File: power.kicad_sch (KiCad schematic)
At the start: 65 parts, among them J5 S7B-XH-A

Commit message: schematic done
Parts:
- removed R34: 0.1m, symbol Device:R
- added BT1: Battery, symbol Device:Battery
- added R34: WSBS8518L1000JK, WSBS8518_VIS, symbol 2026-08-04_01-41-37:WSBS8518L1000JK
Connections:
- net BP-C1M is gone; now on net GND: C54.1, D4.1, J5.7, R20.2, R32.2
- net GND: now also BT1.2 (-), R34.1
- net Pack-: now also R34.2
- net VBAT_24V renamed Pack_24V
- net Pack_24V: now also BT1.1 (+)
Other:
- note added: "Battery plus directly connects to Pack plus"
- note removed: "Pin order needed to be checked"
- note removed: "UPDATE R SHUNT INFO"

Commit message: start to PCB drawing, but error due to missing footprint
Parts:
- R34: footprint WSBS8518_VIS -> MyFootLib:WSBS8518L1000JK
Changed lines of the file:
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@@
 			)
 		)
-		(property "Footprint" "WSBS8518_VIS"
+		(property "Footprint" "MyFootLib:WSBS8518L1000JK"
 			(at 203.2 113.03 0)
 			(hide yes)

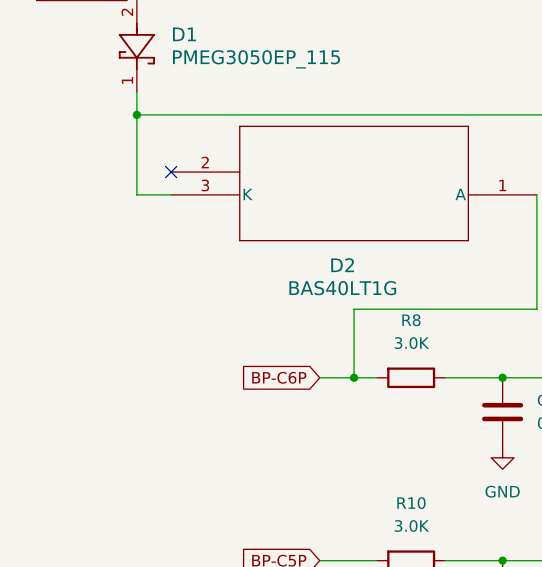
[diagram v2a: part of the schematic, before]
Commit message: feat: CAN/BUCK
1. CAN transceiver added
2. Buck added 24V -> 5V
3. LDO 5V -> 3.3V
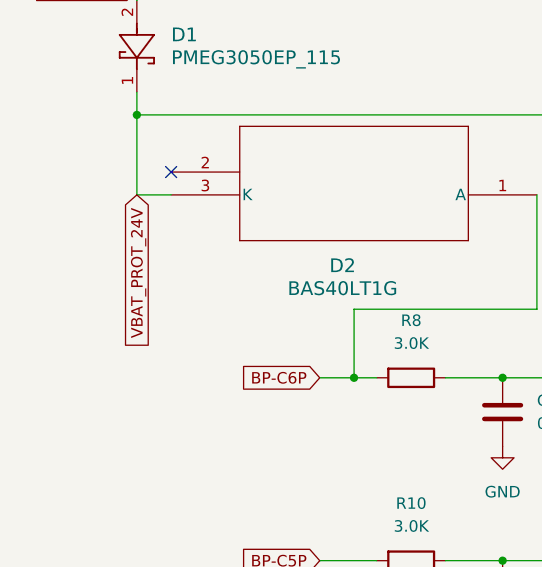
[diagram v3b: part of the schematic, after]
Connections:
- net VBAT_PROT_24V: now reaches C26.1, D1.1, D2.3 (K), R7.1
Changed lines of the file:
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@@
+		)
+	)
+	(global_label "VBAT_PROT_24V"
+		(shape input)
+		(at 26.67 43.18 270)
+		(fields_autoplaced yes)
+		(effects
+			(font
+				(size 1.27 1.27)
+			)
+			(justify right)
+		)
+		(property "Intersheetrefs" "${INTERSHEET_REFS}"
+			(at 26.67 60.8609 90)
+			(hide yes)
+			(show_name no)
+			(do_not_autoplace no)
+			(effects
+				(font
+					(size 1.27 1.27)
+				)
+				(justify right)
+			)
 		)
 	)

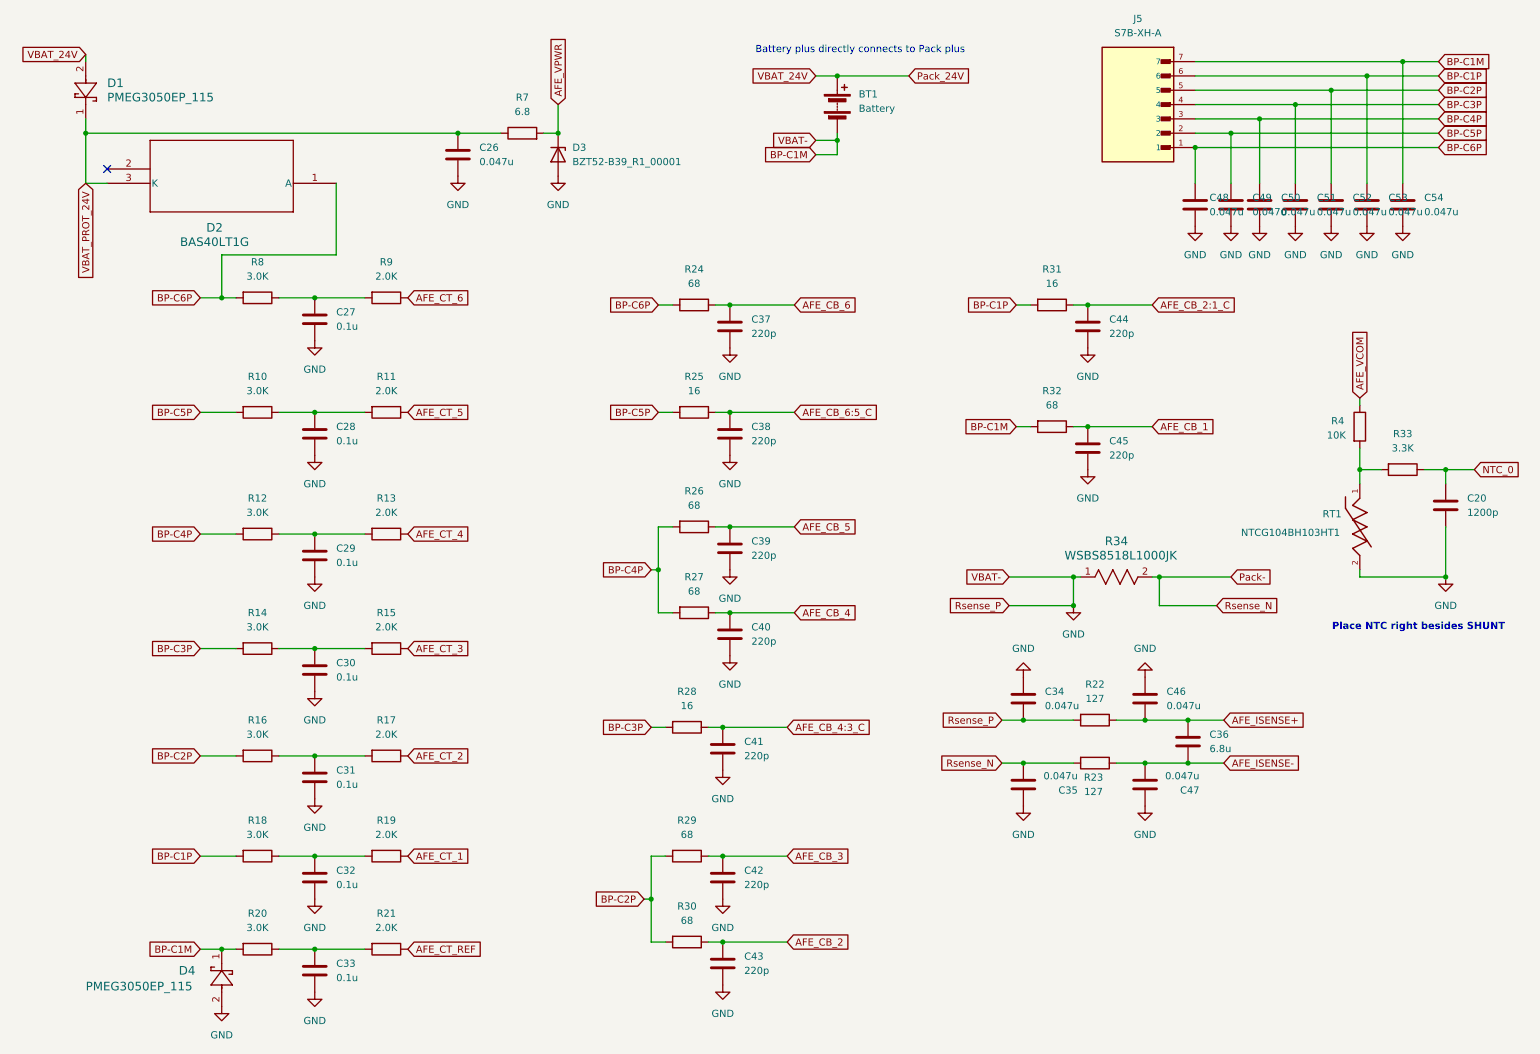
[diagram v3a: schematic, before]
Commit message: fullup the annotation for update PCB from Schematics
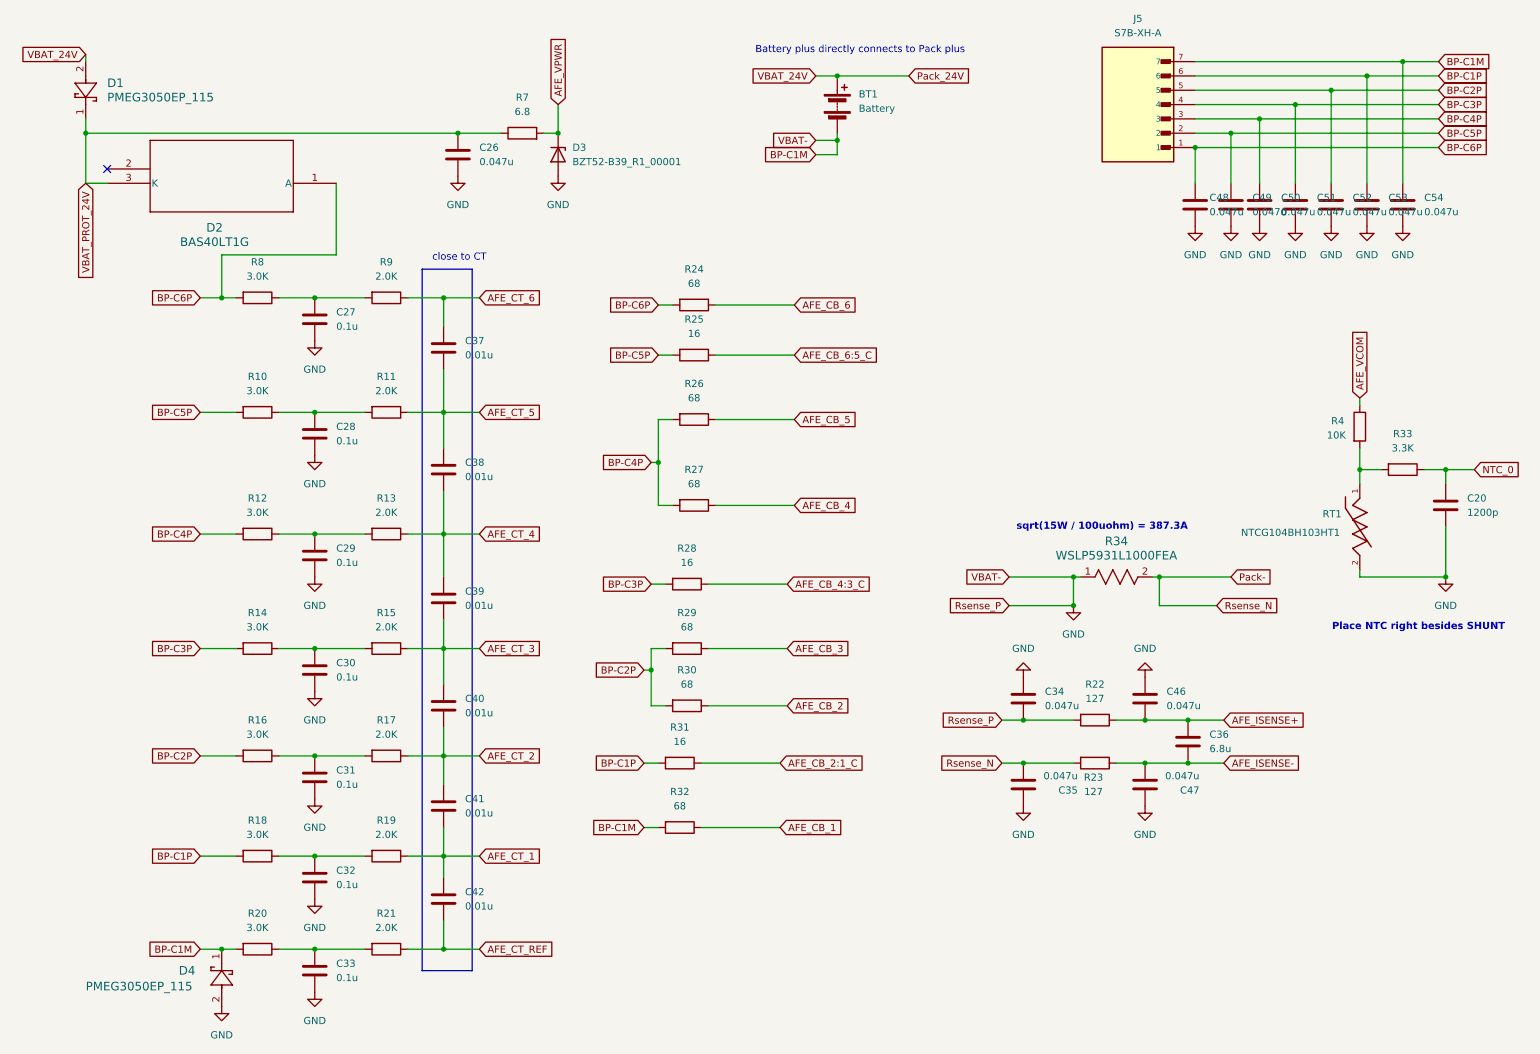
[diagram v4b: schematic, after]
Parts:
- removed C43, C44, C45: 220p, symbol Device:C
- removed R34: WSBS8518L1000JK, MyFootLib:WSBS8518L1000JK, symbol 2026-08-04_01-41-37:WSBS8518L1000JK
- added R34: WSLP5931L1000FEA, WSLP5931L1000FEA, symbol MySym:WSLP5931L1000FEA
- BT1: now left out of the parts list
- C20, C26, C27, C28, C29, C30, C31, C32, C33, C34, C35, C46, C47, C48, C49, C50, C51, C52, C53, C54: footprint (none) -> Capacitor_SMD:C_0402_1005Metric
- C36: footprint (none) -> Capacitor_SMD:C_0603_1608Metric
- C37, C38, C39, C40, C41, C42: value 220p -> 0.01u; footprint (none) -> Capacitor_SMD:C_0402_1005Metric
- D1, D4: footprint SDO_CFP5_SOD128_NEX -> MyFootLib:PMEG3050EP_115
- D2: footprint SOT-23-3_1P4X3P040_ONS -> MyFootLib:BAS40LT1
- J5: footprint S7B-XH-A:JST_S7B-XH-A -> MyFootLib:JST_S7B-XH-A
- R10, R11, R12, R13, R14, R15, R16, R17, R18, R19, R20, R21, R8, R9: footprint (none) -> Resistor_SMD:R_4020_10251Metric
- R22, R23, R33, R4: footprint (none) -> Resistor_SMD:R_0402_1005Metric
- R24, R25, R26, R27, R28, R29, R30, R31, R32: footprint (none) -> Resistor_SMD:R_1206_3216Metric
- R7: footprint (none) -> Resistor_SMD:R_0603_1608Metric
- RT1: footprint NTCG104BH103HT1:THERM_NTCG104BH103HT1 -> MyFootLib:THERM_NTCG104BH103HT1
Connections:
- net AFE_CB_3: no longer C42.1
- net AFE_CB_4: no longer C40.1
- net AFE_CB_4:3_C: no longer C41.1
- net AFE_CB_5: no longer C39.1
- net AFE_CB_6: no longer C37.1
- net AFE_CB_6:5_C: no longer C38.1
- net AFE_CT_1: now also C41.2, C42.1
- net AFE_CT_2: now also C40.2, C41.1
- net AFE_CT_3: now also C39.2, C40.1
- net AFE_CT_4: now also C38.2, C39.1
- net AFE_CT_5: now also C37.2, C38.1
- net AFE_CT_6: now also C37.1
- net AFE_CT_REF: now also C42.2
- net GND: now also R34.1; no longer C37.2, C38.2, C39.2, C40.2, C41.2, C42.2
- net Pack-: now also R34.2
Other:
- note added: "close to CT"
- note added: "sqrt(15W / 100uohm) = 387.3A"
- moved on the sheet: R25, R26, R27, R28, R29, R30, R31, R32

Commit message: update annotation
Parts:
- R34: footprint WSLP5931L1000FEA -> MyFootLib:WSLP5931L1000FEA
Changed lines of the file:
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@@
 			)
 		)
-		(property "Footprint" "WSLP5931L1000FEA"
+		(property "Footprint" "MyFootLib:WSLP5931L1000FEA"
 			(at 203.2 113.03 0)
 			(hide yes)

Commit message: correct R to 0402
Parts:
- R10, R11, R12, R13, R14, R15, R16, R17, R18, R19, R20, R21, R8, R9: footprint Resistor_SMD:R_4020_10251Metric -> Resistor_SMD:R_0402_1005Metric
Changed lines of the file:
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@@
 			)
 		)
-		(property "Footprint" "Resistor_SMD:R_4020_10251Metric"
+		(property "Footprint" "Resistor_SMD:R_0402_1005Metric"
 			(at 80.01 103.632 90)
 			(hide yes)
@@
 			)
 		)
-		(property "Footprint" "Resistor_SMD:R_4020_10251Metric"
+		(property "Footprint" "Resistor_SMD:R_0402_1005Metric"
 			(at 57.15 160.782 90)
 			(hide yes)
@@
 			)
 		)
-		(property "Footprint" "Resistor_SMD:R_4020_10251Metric"
+		(property "Footprint" "Resistor_SMD:R_0402_1005Metric"
 			(at 57.15 143.002 90)
 			(hide yes)
@@
 			)
 		)
-		(property "Footprint" "Resistor_SMD:R_4020_10251Metric"
+		(property "Footprint" "Resistor_SMD:R_0402_1005Metric"
 			(at 80.01 123.952 90)
 			(hide yes)
@@
 			)
 		)
-		(property "Footprint" "Resistor_SMD:R_4020_10251Metric"
+		(property "Footprint" "Resistor_SMD:R_0402_1005Metric"
 			(at 80.01 160.782 90)
 			(hide yes)
@@
 			)
 		)
-		(property "Footprint" "Resistor_SMD:R_4020_10251Metric"
+		(property "Footprint" "Resistor_SMD:R_0402_1005Metric"
 			(at 57.15 82.042 90)
 			(hide yes)
@@
 			)
 		)
-		(property "Footprint" "Resistor_SMD:R_4020_10251Metric"
+		(property "Footprint" "Resistor_SMD:R_0402_1005Metric"
 			(at 57.15 103.632 90)
 			(hide yes)
@@
 			)
 		)
-		(property "Footprint" "Resistor_SMD:R_4020_10251Metric"
+		(property "Footprint" "Resistor_SMD:R_0402_1005Metric"
 			(at 57.15 123.952 90)
 			(hide yes)
@@
 			)
 		)
-		(property "Footprint" "Resistor_SMD:R_4020_10251Metric"
+		(property "Footprint" "Resistor_SMD:R_0402_1005Metric"
 			(at 80.01 177.292 90)
 			(hide yes)
@@
 			)
 		)
-		(property "Footprint" "Resistor_SMD:R_4020_10251Metric"
+		(property "Footprint" "Resistor_SMD:R_0402_1005Metric"
 			(at 57.15 177.292 90)
 			(hide yes)
@@
 			)
 		)
-		(property "Footprint" "Resistor_SMD:R_4020_10251Metric"
+		(property "Footprint" "Resistor_SMD:R_0402_1005Metric"
 			(at 80.01 143.002 90)
 			(hide yes)
@@
 			)
 		)
-		(property "Footprint" "Resistor_SMD:R_4020_10251Metric"
+		(property "Footprint" "Resistor_SMD:R_0402_1005Metric"
 			(at 80.01 82.042 90)
 			(hide yes)
@@
 			)
 		)
-		(property "Footprint" "Resistor_SMD:R_4020_10251Metric"
+		(property "Footprint" "Resistor_SMD:R_0402_1005Metric"
 			(at 80.01 61.722 90)
 			(hide yes)
@@
 			)
 		)
-		(property "Footprint" "Resistor_SMD:R_4020_10251Metric"
+		(property "Footprint" "Resistor_SMD:R_0402_1005Metric"
 			(at 57.15 61.722 90)
 			(hide yes)

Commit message: add pad for B and P
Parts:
- added PAD1, PAD2, PAD3, PAD4: pad, MyFootLib:INPUT_PAD, symbol MyySym:PAD
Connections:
- net GND: now also PAD3.1; no longer C54.1, D4.1, J5.7, R20.2, R32.2
- net Pack-: now also PAD4.1
- net Pack_24V: now also PAD1.1, PAD2.1
- new net BP-C1M: C54.1, D4.1, J5.7, R20.2, R32.2

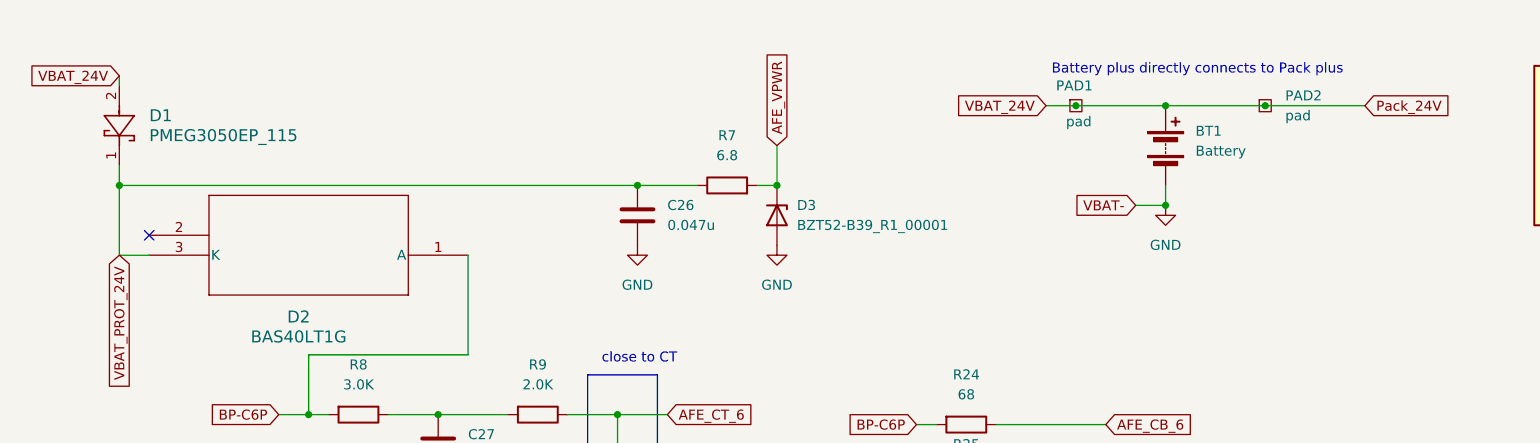
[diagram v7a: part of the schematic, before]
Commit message: GND, power_flag
1. F.Cu and B.Cu fill zone with GND
2. add power_flag
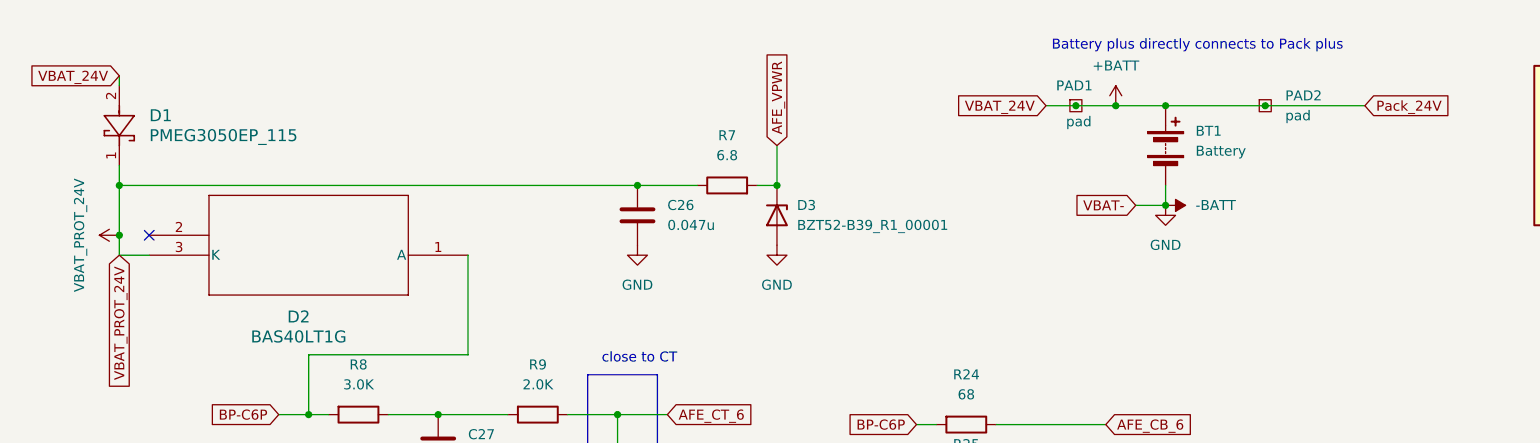
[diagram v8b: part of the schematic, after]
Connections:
- net GND renamed -BATT
- net Pack_24V renamed +BATT
